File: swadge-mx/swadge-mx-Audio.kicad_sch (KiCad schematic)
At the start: 16 parts, among them U2 ES8311

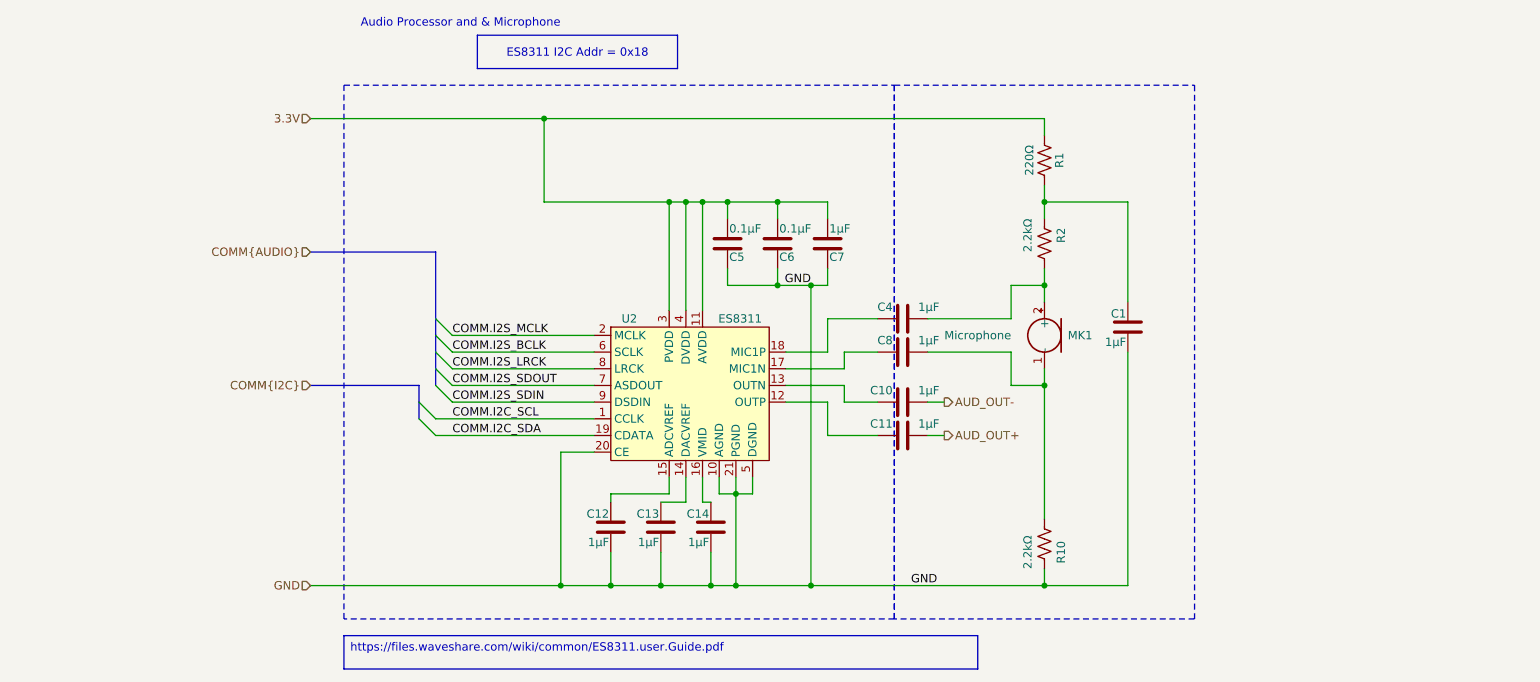
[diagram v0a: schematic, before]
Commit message: Further Subdivide Sheets
Moved all audio into one sheet, and sub-divided into DAC and amp sheets. Moved all power into one sheet and sub-divided into BMS and Buck.
Cleaned up front page a bit.
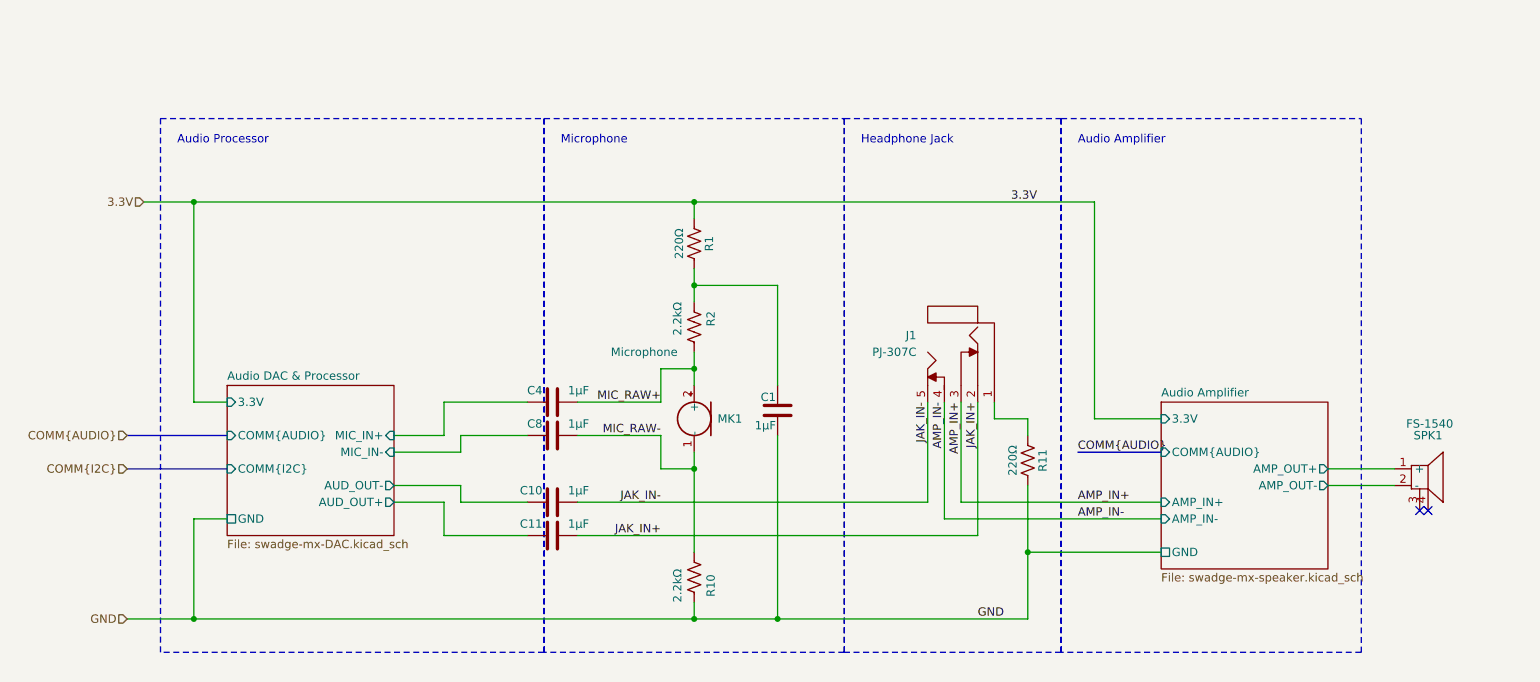
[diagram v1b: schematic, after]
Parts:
- removed C12, C13, C14, C7: 1μF, Swadge_Parts:C_0603_1608Metric, symbol Swadge_Parts:C
- removed C5, C6: 0.1μF, Swadge_Parts:C_0603_1608Metric, symbol Swadge_Parts:C
- removed U2: ES8311, Swadge_Parts:QFN-20-1EP_3x3mm_P0.4mm_EP1.65x1.65mm, symbol Swadge_Parts:ES8311
- added J1: PJ-307C, Swadge_Parts:PJ-307C, symbol Swadge_Parts:PJ-307C
- added R11: 220Ω, Swadge_Parts:R_0603_1608Metric, symbol Swadge_Parts:R_US
- added SPK1: FS-1540, Swadge_Parts:BUZ-SMD_5P-L15.0-W15.0-P13.7-BL, symbol Swadge_Parts:FS-1540
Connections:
- net GND: now also R11.2
- net Audio DAC & Processor/MIC_IN+: now reaches C4.1
- net MIC_RAW+: now reaches C4.2, MK1.2 (+), R2.2
- net Audio DAC & Processor/AUD_OUT+: now reaches C11.1
- net Audio DAC & Processor/AUD_OUT-: now reaches C10.1
- net Audio DAC & Processor/MIC_IN-: now reaches C8.1
- net MIC_RAW-: now reaches C8.2, MK1.1 (-), R10.2
- net AUD_OUT+ renamed JAK_IN+
- net JAK_IN+: now also J1.2
- net AUD_OUT- renamed JAK_IN-
- net JAK_IN-: now also J1.5
- new net: J1.1, R11.1
- new net AMP_IN+: J1.3
- new net AMP_IN-: J1.4
- new net Audio Amplifier/AMP_OUT+: SPK1.1 (+)
- new net Audio Amplifier/AMP_OUT-: SPK1.2 (-)
- no-connect marks 0 -> 2
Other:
- added sheet Audio Amplifier (swadge-mx-speaker.kicad_sch)
- added sheet Audio DAC & Processor (swadge-mx-DAC.kicad_sch)
- note added: "Audio Amplifier"
- note added: "Audio Processor"
- note added: "Headphone Jack"
- note added: "Microphone"
- note removed: "Audio Processor and & Microphone"
- moved on the sheet: C1, C10, C11, C4, C8, MK1, R1, R10, R2

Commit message: Updated power netclass, traces. Switched mic footprint. Added spk terminals
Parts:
- added J8: Conn_01x03_Male, Swadge_Parts:PinHeader_1x03_P2.54mm_Vertical, symbol Swadge_Parts:Conn_01x03_Male
- MK1: footprint Swadge_Parts:INGHAi_MIC_GMI4013S-2C58DB -> Swadge_Parts:MIC-SMD_BD4.0_B4013AM423-093-1
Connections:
- net Audio Amplifier/AMP_OUT+: now also J8.2 (Pin_2)
- net Audio Amplifier/AMP_OUT-: now also J8.3 (Pin_3)
- net GND: now also J8.1 (Pin_1)
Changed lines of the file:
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@@
+	)
+	(junction
+		(at 185.42 114.3)
+		(diameter 0)
+		(color 0 0 0 0)
 	)
 	(junction
@@
 	)
 	(junction
+		(at 238.76 91.44)
+		(diameter 0)
+		(color 0 0 0 0)
+	)
+	(junction
+		(at 237.49 93.98)
+		(diameter 0)
+		(color 0 0 0 0)
+	)
+	(junction
 		(at 134.62 50.8)
 		(diameter 0)
@@
 	(wire
 		(pts
-			(xy 231.14 93.98) (xy 241.3 93.98)
+			(xy 231.14 93.98) (xy 237.49 93.98)
 		)
 		(stroke
@@
 	(wire
 		(pts
+			(xy 238.76 76.2) (xy 238.76 91.44)
+		)
+		(stroke
+			(width 0)
+			(type default)
+		)
+	)
+	(wire
+		(pts
 			(xy 134.62 50.8) (xy 195.58 50.8)
 		)
@@
 	(wire
 		(pts
+			(xy 241.3 73.66) (xy 237.49 73.66)
+		)
+		(stroke
+			(width 0)
+			(type default)
+		)
+	)
+	(wire
+		(pts
 			(xy 134.62 63.5) (xy 134.62 66.04)
 		)
@@
 	(wire
 		(pts
+			(xy 237.49 73.66) (xy 237.49 93.98)
+		)
+		(stroke
+			(width 0)
+			(type default)
+		)
+	)
+	(wire
+		(pts
 			(xy 129.54 81.28) (xy 116.84 81.28)
 		)
@@
 	(wire
 		(pts
+			(xy 238.76 91.44) (xy 241.3 91.44)
+		)
+		(stroke
+			(width 0)
+			(type default)
+		)
+	)
+	(wire
+		(pts
+			(xy 241.3 76.2) (xy 238.76 76.2)
+		)
+		(stroke
+			(width 0)
+			(type default)
+		)
+	)
+	(wire
+		(pts
+			(xy 240.03 78.74) (xy 240.03 114.3)
+		)
+		(stroke
+			(width 0)
+			(type default)
+		)
+	)
+	(wire
+		(pts
 			(xy 96.52 101.6) (xy 96.52 96.52)
 		)
@@
 		)
 	)
+	(wire
+		(pts
+			(xy 237.49 93.98) (xy 241.3 93.98)
+		)
+		(stroke
+			(width 0)
+			(type default)
+		)
+	)
 	(bus
 		(pts
@@
 	(wire
 		(pts
+			(xy 240.03 114.3) (xy 185.42 114.3)
+		)
+		(stroke
+			(width 0)
+			(type default)
+		)
+	)
+	(wire
+		(pts
 			(xy 147.32 63.5) (xy 134.62 63.5)
 		)
@@
 	(wire
 		(pts
+			(xy 241.3 78.74) (xy 240.03 78.74)
+		)
+		(stroke
+			(width 0)
+			(type default)
+		)
+	)
+	(wire
+		(pts
 			(xy 185.42 86.36) (xy 185.42 83.82)
 		)
@@
 	(wire
 		(pts
-			(xy 231.14 91.44) (xy 241.3 91.44)
+			(xy 231.14 91.44) (xy 238.76 91.44)
 		)
 		(stroke
@@
 	)
 	(symbol
+		(lib_id "Swadge_Parts:Conn_01x03_Male")
+		(at 246.38 76.2 180)
+		(unit 1)
+		(exclude_from_sim no)
+		(in_bom yes)
+		(on_board yes)
+		(dnp no)
+		(property "Reference" "J8"
+			(at 246.38 81.28 0)
+			(effects
+				(font
+					(size 1.27 1.27)
+				)
+			)
+		)
+		(property "Value" "Conn_01x03_Male"
+			(at 251.714 71.12 0)
+			(effects
+				(font
+					(size 1.27 1.27)
+				)
+			)
+		)
+		(property "Footprint" "Swadge_Parts:PinHeader_1x03_P2.54mm_Vertical"
+			(at 248.92 78.74 0)
+			(effects
+				(font
+					(size 1.27 1.27)
+				)
+				(hide yes)
+			)
+		)
+		(property "Datasheet" "https://datasheet.lcsc.com/lcsc/1811132313_BOOMELE-Boom-Precision-Elec-C49257_C49257.pdf"
+			(at 246.38 81.28 0)
+			(effects
+				(font
+					(size 1.27 1.27)
+				)
+				(hide yes)
+			)
+		)
+		(property "Description" "Generic connector, single row, 01x03, script generated (kicad-library-utils/schlib/autogen/connector/)"
+			(at 246.38 76.2 0)
+			(effects
+				(font
+					(size 1.27 1.27)
+				)
+				(hide yes)
+			)
+		)
+		(property "Digikey" "1849-1003-ND"
+			(at 243.84 83.82 0)
+			(effects
+				(font
+					(size 1.27 1.27)
+				)
+				(hide yes)
+			)
+		)
+		(property "Substitutable" "Y"
+			(at 238.76 88.9 0)
+			(effects
+				(font
+					(size 1.27 1.27)
+				)
+				(hide yes)
+			)
+		)
+		(property "Notes" "Put a jumper on this, similar to QPC02SXGN-RC"
+			(at 246.38 76.2 0)
+			(effects
+				(font
+					(size 1.27 1.27)
+				)
+				(hide yes)
+			)
+		)
+		(property "LCSC" "C49257"
+			(at 246.38 76.2 0)
+			(effects
+				(font
+					(size 1.27 1.27)
+				)
+				(hide yes)
+			)
+		)
+		(property "Cost@2500" "0.0122"
+			(at 246.38 76.2 0)
+			(effects
+				(font
+					(size 1 1)
+				)
+				(hide yes)
+			)
+		)
+		(pin "1"
+		)
+		(pin "3"
+		)
+		(pin "2"
+		)
+		(instances
+			(project "swadge-mx"
+				(path "/71d9b0a5-2583-445f-b3de-7fdf7b78df55/ad5e1c1f-939a-4ebe-bd0b-e61cbc16b2f8"
+					(reference "J8")
+					(unit 1)
+				)
+			)
+		)
+	)
+	(symbol
 		(lib_name "C_22")
 		(lib_id "Swadge_Parts:C")
@@
 			)
 		)
-		(property "Footprint" "Swadge_Parts:INGHAi_MIC_GMI4013S-2C58DB"
+		(property "Footprint" "Swadge_Parts:MIC-SMD_BD4.0_B4013AM423-093-1"
 			(at 124.46 73.66 90)
 			(effects

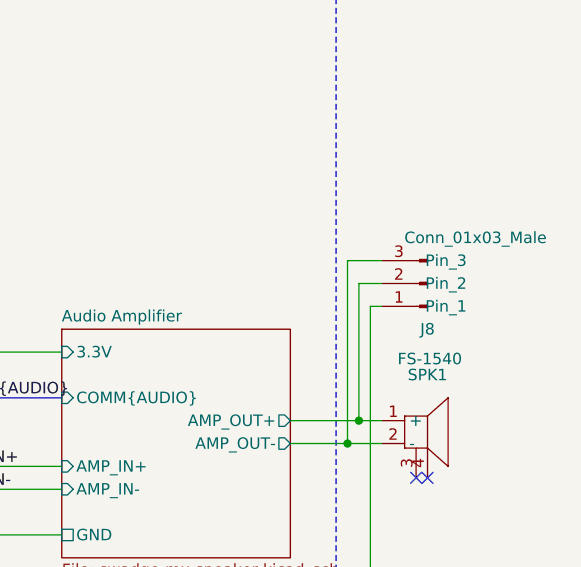
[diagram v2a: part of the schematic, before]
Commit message: #4 Normalize button symbols, fix J8 attributes
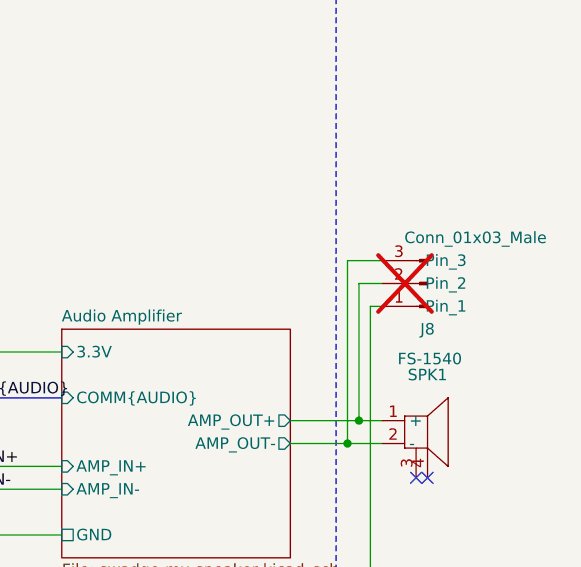
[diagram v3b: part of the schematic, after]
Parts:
- J8: now not fitted; now left out of the parts list
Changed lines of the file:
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@@
 		(unit 1)
 		(exclude_from_sim no)
-		(in_bom yes)
+		(in_bom no)
 		(on_board yes)
-		(dnp no)
+		(dnp yes)
 		(property "Reference" "J8"
 			(at 246.38 81.28 0)
